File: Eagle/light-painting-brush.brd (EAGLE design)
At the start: 24 parts, among them IC1 TPS61070DDC, T1 2N3904, T2 2N3904, T3 2N3904

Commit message: Remove TPS61070 boost converter
Previous version of the board is saved in the "tps61070" branch.
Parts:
- removed C2, C3: 10μ, rcl:C1206
- removed IC1: TPS61070DDC, Gumix:TSOT23-6_DDC
- removed L1: 4.7μ, inductor-sumida:CR43
- removed R10: 220k, resistor:R1206
- removed R9: 1.5M, resistor:R1206
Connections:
- removed net N$13: IC1.1, L1.2
- removed net N$14: IC1.4, R10.1, R9.2
- net GND: no longer C2.2, C3.2, IC1.2, R10.2
- net V+: no longer C2.1, C3.1, IC1.3, IC1.5, IC1.6, L1.1, R9.1
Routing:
- net V+: track 120.2 -> 85.7 mm
- net GND: track 120.5 -> 99.2 mm
- net N$14: track 13.3 -> 0.00 mm, vias 2 -> 0
- net N$13: track 10.0 -> 0.00 mm
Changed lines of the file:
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@@
 <attribute name="VALUE" x="37.973" y="3.048" size="1.27" layer="27" rot="R90"/>
-</element>
-<element name="L1" library="inductor-sumida" package="CR43" value="4.7μ" x="3.175" y="5.08" smashed="yes">
-<attribute name="NAME" x="0.9525" y="8.5725" size="1.016" layer="25" ratio="18"/>
-<attribute name="VALUE" x="0.9525" y="0.9525" size="0.8128" layer="27" ratio="10"/>
-</element>
-<element name="IC1" library="Gumix" package="TSOT23-6_DDC" value="TPS61070DDC" x="11.43" y="4.445" smashed="yes">
-<attribute name="MF" value="" x="11.43" y="4.445" size="1.778" layer="27" display="off"/>
-<attribute name="MPN" value="TPS61070DDCR" x="11.43" y="4.445" size="1.778" layer="27" display="off"/>
-<attribute name="NAME" x="10.16" y="6.35" size="1.27" layer="25"/>
-<attribute name="OC_FARNELL" value="1461062" x="11.43" y="4.445" size="1.778" layer="27" display="off"/>
-<attribute name="OC_NEWARK" value="64M3125" x="11.43" y="4.445" size="1.778" layer="27" display="off"/>
-<attribute name="VALUE" x="10.16" y="1.27" size="1.27" layer="27"/>
-</element>
-<element name="R9" library="resistor" package="R1206" value="1.5M" x="10.16" y="10.16" smashed="yes">
-<attribute name="NAME" x="8.763" y="11.303" size="1.27" layer="25"/>
-<attribute name="VALUE" x="8.763" y="7.747" size="1.27" layer="27"/>
-</element>
-<element name="R10" library="resistor" package="R1206" value="220k" x="17.78" y="10.16" smashed="yes">
-<attribute name="NAME" x="16.383" y="11.303" size="1.27" layer="25"/>
-<attribute name="VALUE" x="16.383" y="7.747" size="1.27" layer="27"/>
-</element>
-<element name="C2" library="rcl" package="C1206" value="10μ" x="7.62" y="5.715" smashed="yes" rot="R270">
-<attribute name="NAME" x="8.89" y="6.985" size="1.27" layer="25" rot="R270"/>
-<attribute name="VALUE" x="5.08" y="6.985" size="1.27" layer="27" rot="R270"/>
-</element>
-<element name="C3" library="rcl" package="C1206" value="10μ" x="17.145" y="5.715" smashed="yes" rot="R270">
-<attribute name="NAME" x="18.415" y="6.985" size="1.27" layer="25" rot="R270"/>
-<attribute name="VALUE" x="14.605" y="6.985" size="1.27" layer="27" rot="R270"/>
 </element>
 <element name="LSP1" library="solpad" package="LSP10" value="LSP10" x="1.905" y="10.16" smashed="yes">
@@
 <contactref element="D1" pad="CATHODE2"/>
 <contactref element="D1" pad="CATHODE1"/>
-<contactref element="R10" pad="2"/>
-<contactref element="IC1" pad="2"/>
-<contactref element="C2" pad="2"/>
-<contactref element="C3" pad="2"/>
 <contactref element="S1" pad="2"/>
 <contactref element="S2" pad="2"/>
@@
 <contactref element="S2" pad="1"/>
 <contactref element="LSP2" pad="MP"/>
-<wire x1="11.43" y1="3.195" x2="11.43" y2="4.445" width="0.6" layer="1"/>
-<wire x1="11.43" y1="4.445" x2="7.62" y2="4.445" width="0.6" layer="1"/>
-<wire x1="11.43" y1="3.195" x2="11.43" y2="1.905" width="0.6" layer="1"/>
-<wire x1="17.145" y1="3.81" x2="17.145" y2="4.315" width="0.6" layer="1"/>
 <wire x1="19.93" y1="1.56" x2="24.13" y2="1.56" width="1.4" layer="1"/>
 <wire x1="24.13" y1="1.56" x2="28.33" y2="1.56" width="1.4" layer="1"/>
 <wire x1="19.93" y1="1.56" x2="17.145" y2="1.56" width="1.4" layer="1"/>
 <wire x1="17.145" y1="1.56" x2="17.145" y2="1.905" width="1.4" layer="1"/>
-<wire x1="17.145" y1="1.905" x2="17.145" y2="3.81" width="1.4" layer="1"/>
-<wire x1="17.145" y1="1.905" x2="13.97" y2="1.905" width="1" layer="1"/>
-<wire x1="13.97" y1="1.905" x2="12.065" y2="1.905" width="1" layer="1"/>
-<wire x1="11.43" y1="1.905" x2="13.97" y2="1.905" width="0.6" layer="1"/>
-<wire x1="19.202" y1="10.16" x2="24.13" y2="10.16" width="1.4" layer="1"/>
 <wire x1="24.13" y1="10.16" x2="24.13" y2="1.56" width="1.4" layer="1"/>
 <wire x1="42.3" y1="15.53" x2="38.1" y2="15.53" width="1.4" layer="1"/>
@@
 <wire x1="32.385" y1="27.305" x2="38.1" y2="21.59" width="1" layer="1"/>
 <wire x1="38.1" y1="21.59" x2="38.1" y2="15.53" width="1" layer="1"/>
-<wire x1="17.145" y1="1.56" x2="17.78" y2="1.56" width="0" layer="19" extent="1-16"/>
-<wire x1="7.62" y1="4.315" x2="7.62" y2="4.445" width="0" layer="19" extent="1-1"/>
+<wire x1="17.145" y1="1.905" x2="17.78" y2="1.56" width="0" layer="19" extent="16-16"/>
 </signal>
 <signal name="N$1">
@@
 <contactref element="R8" pad="1"/>
 <contactref element="T3" pad="1"/>
-<contactref element="L1" pad="1"/>
-<contactref element="C2" pad="1"/>
-<contactref element="IC1" pad="6"/>
-<contactref element="IC1" pad="3"/>
-<contactref element="IC1" pad="5"/>
-<contactref element="R9" pad="1"/>
-<contactref element="C3" pad="1"/>
 <contactref element="R2" pad="1"/>
 <contactref element="R3" pad="1"/>
 <contactref element="LSP1" pad="MP"/>
-<wire x1="11.43" y1="5.695" x2="11.43" y2="6.985" width="0.6" layer="1"/>
-<wire x1="11.43" y1="6.985" x2="10.48" y2="6.985" width="0.6" layer="1"/>
-<wire x1="10.48" y1="6.985" x2="10.48" y2="5.695" width="0.6" layer="1"/>
-<wire x1="11.43" y1="7.115" x2="11.43" y2="6.985" width="0.6" layer="1"/>
-<wire x1="17.145" y1="7.115" x2="15.24" y2="7.115" width="0.6" layer="1"/>
-<wire x1="2.54" y1="7.115" x2="2.5885625" y2="7.093203125" width="0.6" layer="1"/>
-<wire x1="2.5885625" y1="7.093203125" x2="3.175" y2="6.83" width="0.6" layer="1"/>
-<wire x1="12.38" y1="3.195" x2="15.24" y2="3.195" width="0.6" layer="1"/>
-<wire x1="15.24" y1="3.195" x2="15.24" y2="7.115" width="0.6" layer="1"/>
-<wire x1="7.62" y1="7.115" x2="2.5885625" y2="7.115" width="1.4" layer="1"/>
-<wire x1="2.5885625" y1="7.115" x2="2.5885625" y2="7.093203125" width="1.4" layer="1"/>
-<wire x1="11.43" y1="7.115" x2="17.145" y2="7.115" width="1.4" layer="1"/>
-<wire x1="7.62" y1="7.115" x2="8.89" y2="7.115" width="1.4" layer="1"/>
-<wire x1="8.89" y1="7.115" x2="11.43" y2="7.115" width="1.4" layer="1"/>
-<wire x1="8.738" y1="10.16" x2="8.89" y2="10.16" width="1.3" layer="1"/>
-<wire x1="8.89" y1="10.16" x2="8.89" y2="7.115" width="1.3" layer="1"/>
-<wire x1="2.5885625" y1="7.115" x2="1.905" y2="7.115" width="2" layer="1"/>
-<wire x1="1.905" y1="7.115" x2="1.905" y2="10.16" width="2" layer="1"/>
 <wire x1="1.905" y1="20.32" x2="1.905" y2="16.358" width="1.4" layer="1"/>
 <wire x1="1.905" y1="16.358" x2="1.905" y2="13.335" width="1.4" layer="1"/>
@@
 <wire x1="39.37" y1="12.7" x2="21.59" y2="31.49" width="0" layer="19" extent="16-16"/>
 </signal>
-<signal name="N$13">
-<contactref element="L1" pad="2"/>
-<contactref element="IC1" pad="1"/>
-<wire x1="3.175" y1="3.33" x2="5.08" y2="3.33" width="0.6" layer="1"/>
-<wire x1="5.08" y1="3.33" x2="5.08" y2="1.905" width="0.6" layer="1"/>
-<wire x1="5.08" y1="1.905" x2="10.48" y2="1.905" width="0.6" layer="1"/>
-<wire x1="10.48" y1="1.905" x2="10.48" y2="3.195" width="0.6" layer="1"/>
-</signal>
-<signal name="N$14">
-<contactref element="R9" pad="2"/>
-<contactref element="R10" pad="1"/>
-<contactref element="IC1" pad="4"/>
-<via x="13.97" y="9.525" extent="1-16" drill="0.6" diameter="0.8128"/>
-<via x="13.97" y="4.445" extent="1-16" drill="0.6" diameter="0.8128"/>
-<wire x1="13.97" y1="9.525" x2="13.97" y2="4.445" width="0.6" layer="16"/>
-<wire x1="12.38" y1="5.695" x2="13.97" y2="5.695" width="0.6" layer="1"/>
-<wire x1="13.97" y1="5.695" x2="13.97" y2="4.445" width="0.6" layer="1"/>
-<wire x1="11.582" y1="10.16" x2="13.97" y2="10.16" width="1.4" layer="1"/>
-<wire x1="13.97" y1="10.16" x2="16.358" y2="10.16" width="1.4" layer="1"/>
-<wire x1="13.97" y1="9.525" x2="13.97" y2="10.16" width="0.6" layer="1"/>
-</signal>
 <signal name="N$15">

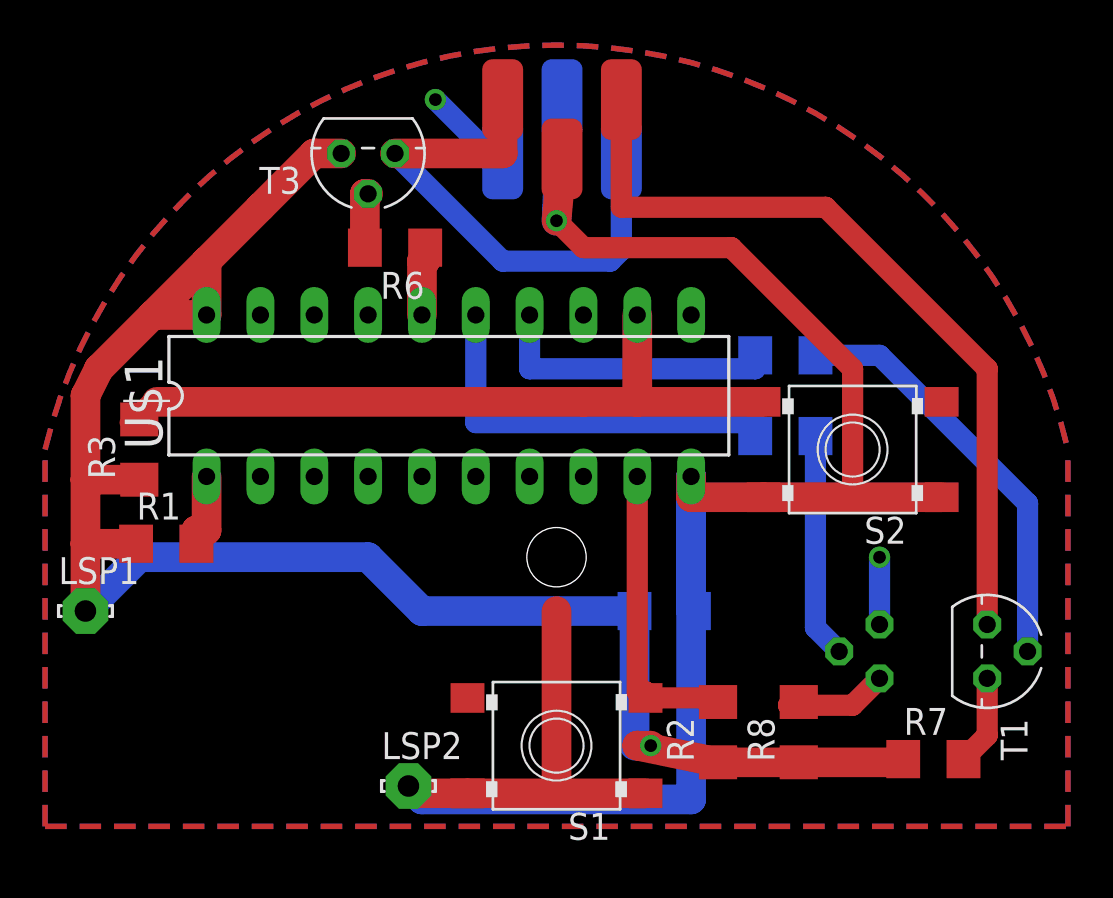
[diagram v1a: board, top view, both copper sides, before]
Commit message: Redesign the PCB assuming 4V input
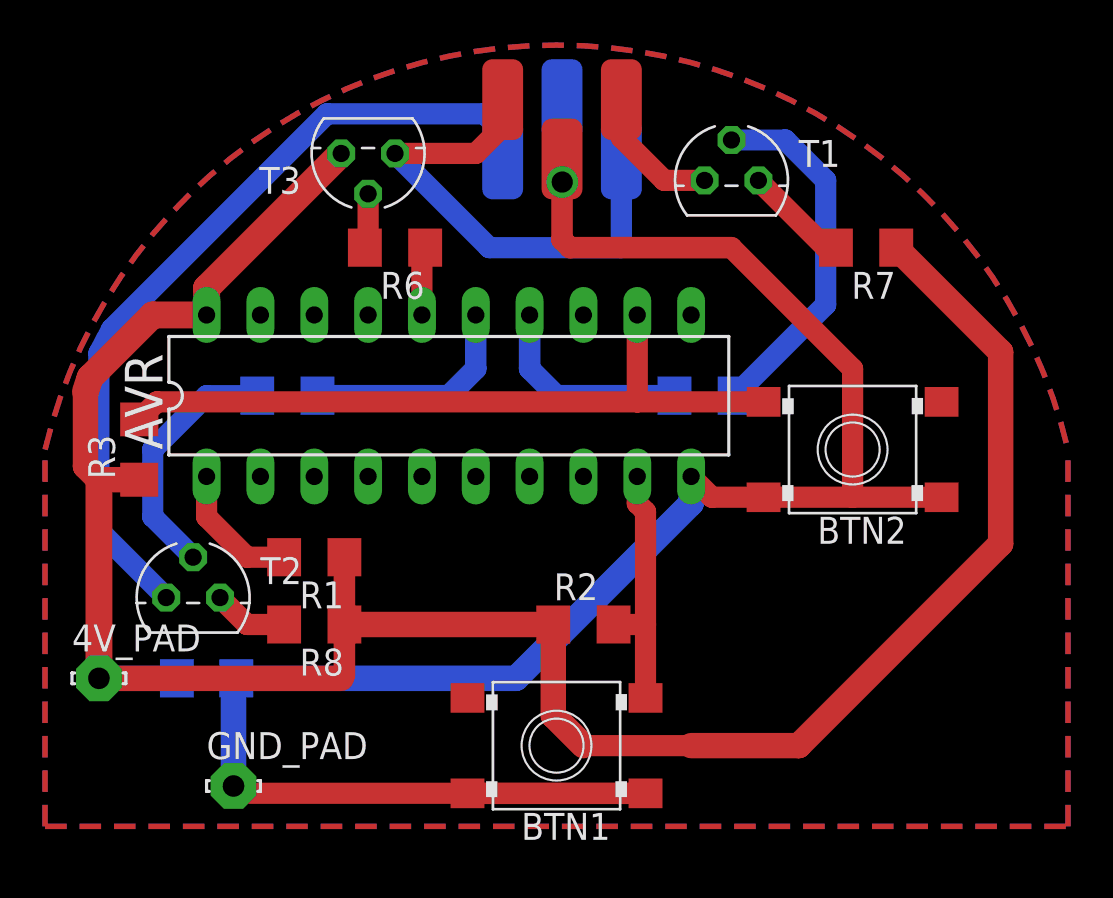
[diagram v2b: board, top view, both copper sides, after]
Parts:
- removed LSP1, LSP2: LSP10, solpad:LSP10
- added 4V_PAD, GND_PAD: LSP10, solpad:LSP10
- R8: value 100 -> 90
- moved T2 32.5 mm to (6.99, 10.8), flipped to the top, turned to 0 degrees
- moved T1 25.3 mm to (32.4, 30.5), turned to 0 degrees
- moved R7 24.3 mm to (38.7, 27.3), turned to 180 degrees
- moved R5 23.6 mm to (11.4, 20.3), turned to 0 degrees
- moved R8 23.4 mm to (12.7, 9.53), turned to 180 degrees
- moved C1 21.8 mm to (7.62, 6.99)
- moved R2 8.13 mm to (25.4, 9.53), turned to 0 degrees
- moved R1 7.01 mm to (12.7, 12.7), turned to 180 degrees
- moved R4 4.26 mm to (31.1, 20.3)
- renumbered S1 to BTN1, S2 to BTN2, U$1 to AVR
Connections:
- net N$10 renamed BLUE0
- net N$2 renamed RED
- net N$3 renamed GREEN
- net N$4 renamed BLUE
- net N$8 renamed RED0
- net N$9 renamed GREEN0
- removed net V+: AVR.20, C1.1, LSP1.MP, R1.1, R2.1, R3.1, R7.1, R8.1, T3.1
- new net VCC: 4V_PAD.MP, AVR.20, C1.1, R1.1, R2.1, R3.1, R7.1, R8.1, T3.1
- net GND: now also GND_PAD.MP; no longer LSP2.MP
- net N$15: now also BTN1.4
- net N$16: now also BTN2.3
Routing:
- net VCC: track 0.00 -> 110.1 mm
- net V+: track 85.7 -> 0.00 mm, vias 1 -> 0
- net GREEN: track 7.66 -> 38.7 mm, vias 2 -> 0
- net RED: track 37.6 -> 6.55 mm
- net GREEN0: track 18.9 -> 10.5 mm
- net GND: track 99.2 -> 94.2 mm
- net RED0: track 13.8 -> 9.90 mm
- net N$5: track 19.9 -> 17.2 mm
- net N$1: track 3.66 -> 6.35 mm
- net N$15: track 14.3 -> 12.2 mm
- net N$17: track 1.80 -> 0.00 mm
- net N$12: track 5.33 -> 3.55 mm
- net N$16: track 32.7 -> 34.3 mm
- net BLUE: track 24.9 -> 23.6 mm
- net N$6: track 10.6 -> 11.8 mm
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
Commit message: Move C1 closer to VCC and GND pins of AVR
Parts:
- moved R3 35.9 mm to (39.4, 9.53)
- moved C1 14.5 mm to (13.3, 20.3), flipped to the top, turned to 0 degrees
- moved 4V_PAD 11.6 mm to (14.0, 5.08)
- moved GND_PAD 7.62 mm to (16.5, 1.91)
- moved R4 3.81 mm to (27.3, 20.3)
- moved R5 1.91 mm to (13.3, 20.3)
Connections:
- net N$11 renamed RED2
- net N$12 renamed GREEN2
- net N$5 renamed RED1
- net N$6 renamed GREEN1
- net N$7 renamed BLUE1
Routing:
- net N$16: track 34.3 -> 19.6 mm
- net GND: track 94.2 -> 86.5 mm
- net RED0: track 9.90 -> 6.09 mm
- net RED1: track 17.2 -> 19.6 mm
- net GREEN1: track 11.8 -> 13.8 mm
- net GREEN0: track 10.5 -> 8.63 mm

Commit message: Update values assuming 5V input
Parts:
- R6: value 5.6k -> 10k
- R8: value 90 -> 100
- renumbered 4V_PAD to 5V_PAD
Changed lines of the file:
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@@
 <attribute name="VALUE" x="12.065" y="33.02" size="1.27" layer="27" ratio="10" rot="R180"/>
 </element>
-<element name="R6" library="resistor" package="R1206" value="5.6k" x="16.51" y="27.305" smashed="yes" rot="R180">
+<element name="R6" library="resistor" package="R1206" value="10k" x="16.51" y="27.305" smashed="yes" rot="R180">
 <attribute name="NAME" x="17.907" y="26.162" size="1.27" layer="25" rot="R180"/>
 <attribute name="VALUE" x="17.907" y="29.718" size="1.27" layer="27" rot="R180"/>
@@
 <attribute name="VALUE" x="40.132" y="29.718" size="1.27" layer="27" rot="R180"/>
 </element>
-<element name="R8" library="resistor" package="R1206" value="90" x="12.7" y="9.525" smashed="yes" rot="R180">
+<element name="R8" library="resistor" package="R1206" value="100" x="12.7" y="9.525" smashed="yes" rot="R180">
 <attribute name="NAME" x="14.097" y="8.382" size="1.27" layer="25" rot="R180"/>
 <attribute name="VALUE" x="14.097" y="11.938" size="1.27" layer="27" rot="R180"/>
 </element>
-<element name="4V_PAD" library="solpad" package="LSP10" value="LSP10" x="13.97" y="5.08" smashed="yes">
+<element name="5V_PAD" library="solpad" package="LSP10" value="LSP10" x="13.97" y="5.08" smashed="yes">
 <attribute name="NAME" x="12.7" y="6.35" size="1.27" layer="25" ratio="10"/>
 <attribute name="VALUE" x="13.97" y="5.334" size="0.0254" layer="27"/>
@@
 <contactref element="R8" pad="1"/>
 <contactref element="T3" pad="1"/>
-<contactref element="4V_PAD" pad="MP"/>
+<contactref element="5V_PAD" pad="MP"/>
 <wire x1="25.4" y1="3.81" x2="29.21" y2="3.81" width="1" layer="1"/>
 <wire x1="29.21" y1="3.81" x2="30.48" y2="3.81" width="1" layer="1"/>
